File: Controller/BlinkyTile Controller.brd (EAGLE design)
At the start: 78 x 30 mm, 27 parts, among them IC1 74LVC1G17DCK, IC2 74LVC1G17DCK, Q1 CRYSTAL_4PAD2520, SW1 SPST_TACT-EVQQ2, SW2 SPST_TACT-EVQQ2, T1 TEST_PAD-7, T2 TEST_PAD-7, U1 MK20DX128VLF5

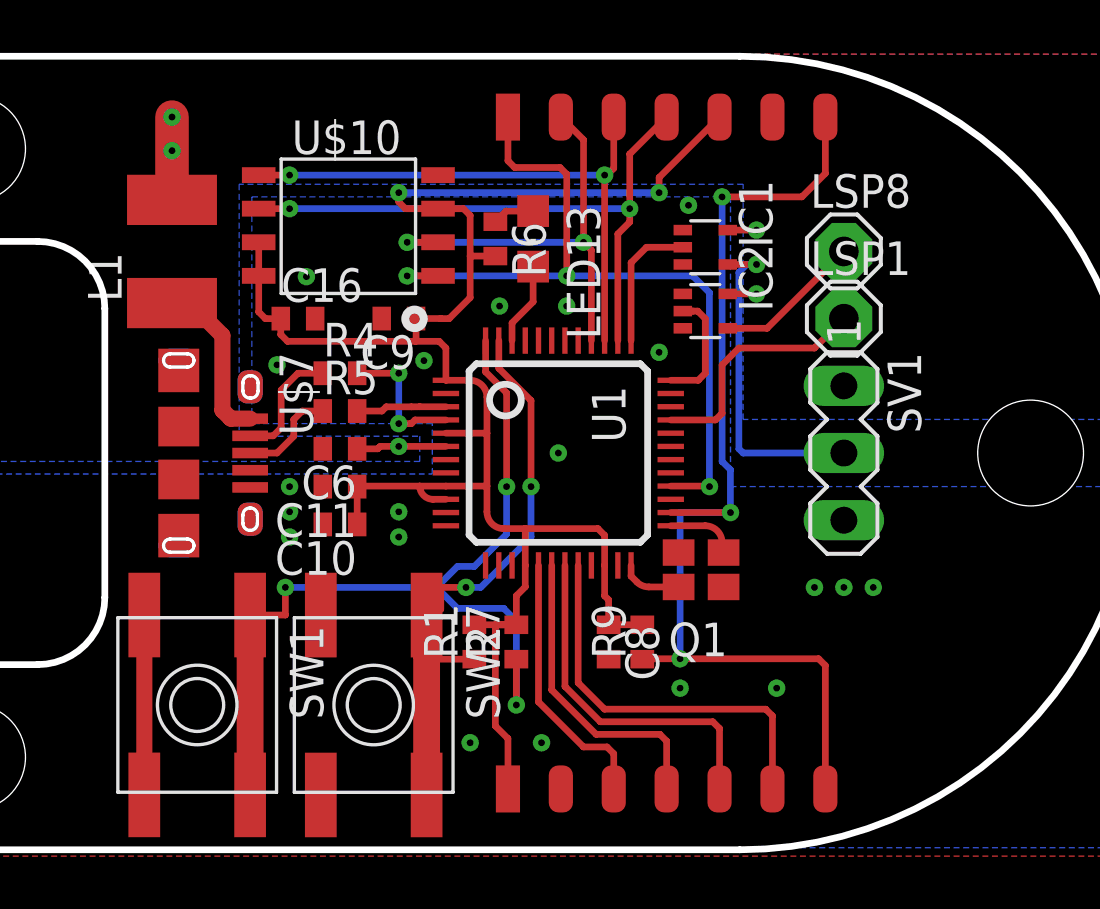
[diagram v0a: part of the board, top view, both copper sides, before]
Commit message: Update controller board design for RevA
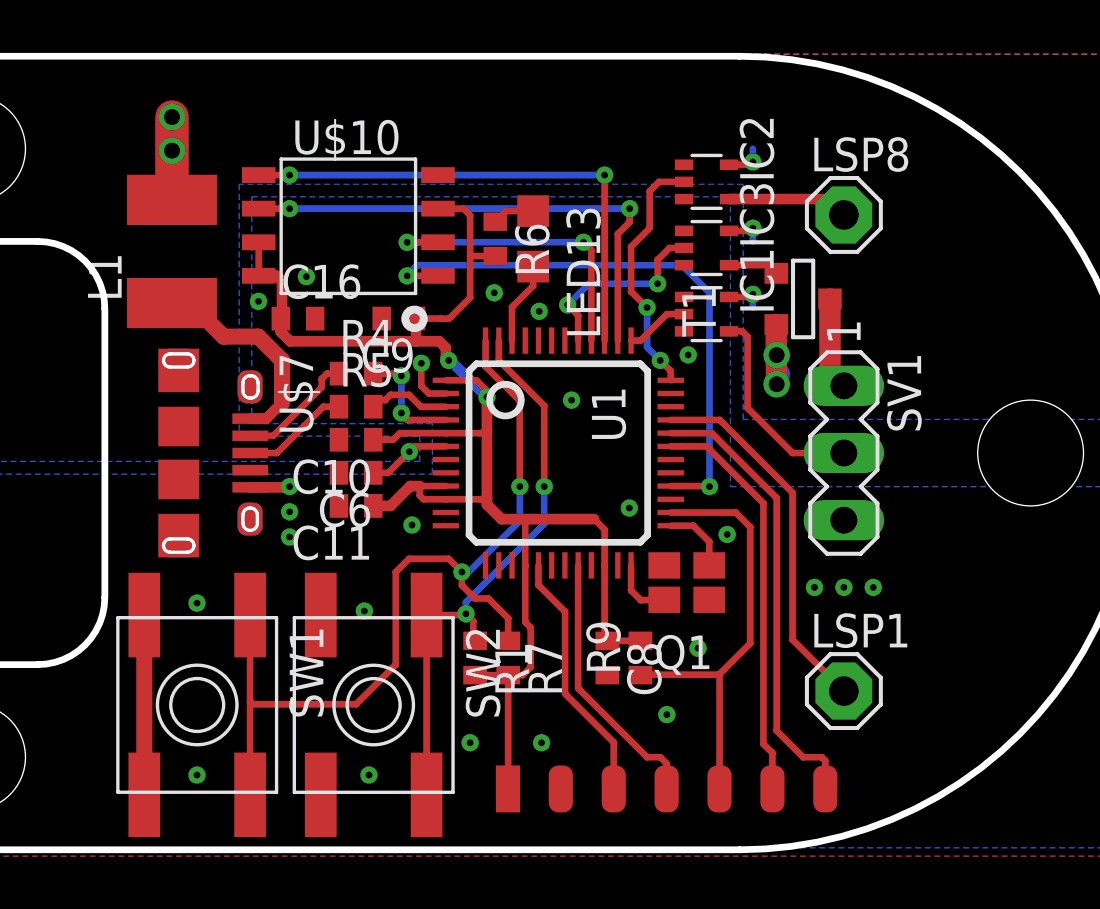
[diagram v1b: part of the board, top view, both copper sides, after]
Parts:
- added IC3: 74LVC1G17DCK, 74xx-little-us:SC70-5
- C10, C11, C16, C6, C8, C9: device rcl:C0402 -> adafruit:C0402
- R1, R4, R5, R6, R7, R9: device rcl:R0402 -> adafruit:R0402
- T1: value TEST_PAD-7 -> (none); device Sam Library:TEST_PAD-7 -> zetex:SOT-23
- moved LSP1 14.1 mm to (27.9, -9.00)
- moved T1 13.1 mm to (26.4, 5.80), turned to 90 degrees
- moved IC2 4.88 mm to (22.8, 10.2)
- moved C10 3.26 mm to (9.50, 0.50)
- moved IC1 2.53 mm to (22.8, 5.25)
- moved LSP8 1.38 mm to (27.9, 9.00)
- moved C6 1.09 mm to (9.50, -0.75)
- moved C11 0.95 mm to (9.50, -2.00)
- moved Q1 0.73 mm to (22.0, -4.90)
- moved R7 0.68 mm to (15.2, -7.75), turned to 270 degrees
- moved R5 0.63 mm to (9.50, 1.75)
- moved R9 0.61 mm to (20.2, -7.75)
- moved R4 0.61 mm to (9.50, 3.00)
- moved C8 0.61 mm to (19.0, -7.75)
- moved R1 0.61 mm to (14.0, -7.75), turned to 270 degrees
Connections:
- net ADDR_PROG renamed ADDRESS_PROGRAM
- new net N$5: SV1.1, T1.1
- new net N$6: IC3.4, T1.3
- new net POWER_ENABLE: IC3.2, U1.41
- net +3V3: no longer T1.5
- net +5V: now also IC3.5, T1.2; no longer SV1.1
- net FLASH_CS: no longer T1.1
- net FLASH_MISO: no longer T1.2
- net FLASH_MOSI: no longer T1.3
- net FLASH_SCK: no longer T1.4
- net GND: now also IC3.3; no longer T1.6
- net RESET: now also T2.5; no longer T1.7, T2.7
- net RX: now also T2.6
- net TDI: no longer T2.4
- net TDO: no longer T2.5
- net TMS: now also T2.4; no longer T2.6
- net TX: now also T2.7
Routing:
- net RESET: track 39.9 -> 16.6 mm, vias 3 -> 0
- net TX: track 0.00 -> 17.2 mm
- net RX: track 0.00 -> 15.3 mm
- net TDO: track 13.4 -> 0.00 mm
- net +3V3: track 73.4 -> 60.9 mm
- net TDI: track 11.7 -> 0.00 mm
- net FLASH_CS: track 29.6 -> 22.0 mm, vias 3 -> 2
- net POWER_ENABLE: track 0.00 -> 7.33 mm, vias 0 -> 2
- net FLASH_MISO: track 16.8 -> 11.7 mm
- net TMS: track 15.1 -> 10.1 mm
- net ADC1: track 9.20 -> 14.0 mm
- net LED_DATA: track 12.6 -> 7.83 mm, vias 1 -> 0
- net ADDRESS_PROGRAM: track 4.85 -> 9.51 mm, vias 0 -> 2
- net +5V: track 8.70 -> 13.3 mm, vias 5 -> 8
- net FLASH_SCK: track 23.2 -> 19.2 mm
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
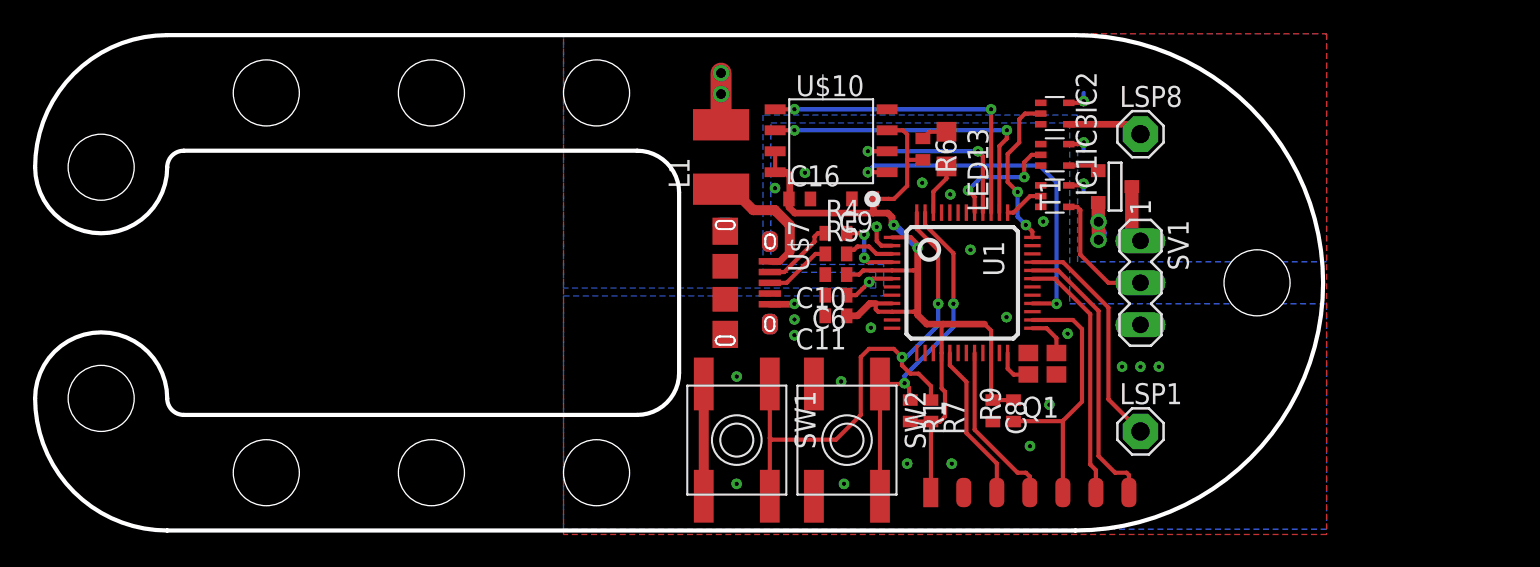
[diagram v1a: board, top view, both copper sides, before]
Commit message: Switch to smaller processor, change FLASH_CS to hardware CS pin
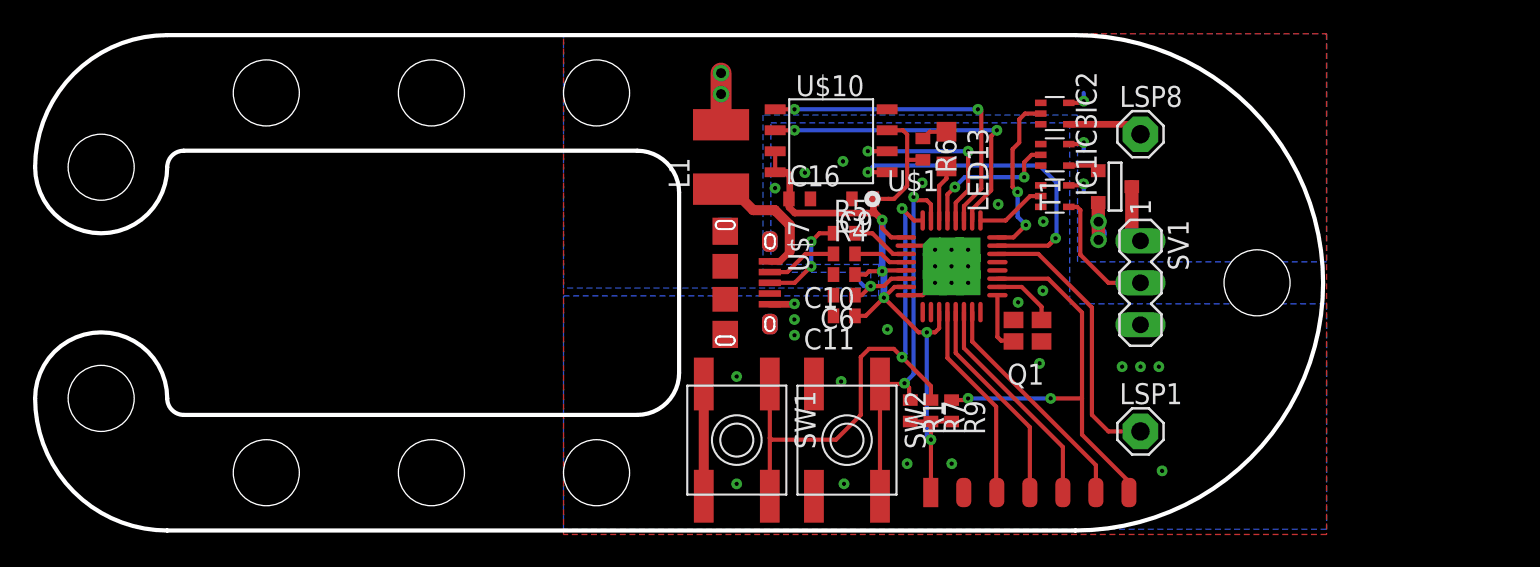
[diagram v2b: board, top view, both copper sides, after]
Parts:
- removed C8: 100nF, adafruit:C0402
- removed U1: MK20DX128VLF5, scanlime:LQFP48
- added U$1: MK20D--VFM5, blinkinlabs:QFN32_5X5_LONGLEADS
- moved R9 3.75 mm to (16.5, -7.75), turned to 270 degrees
- moved Q1 2.19 mm to (21.1, -2.90)
- moved R4 1.35 mm to (10.0, 1.75)
- moved R5 1.35 mm to (10.0, 3.00)
- moved C10 0.50 mm to (10.0, 0.50)
- moved C11 0.50 mm to (10.0, -2.00)
- moved C6 0.50 mm to (10.0, -0.75)
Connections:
- removed net ADC1: LSP1.MP, U1.33
- removed net TDI: U1.18
- removed net TDO: U1.19
- new net ADC15: LSP1.MP, U$1.22
- net +3V3: now also U$1.1, U$1.11, U$1.5, U$1.7; no longer C8.1, U1.1, U1.10, U1.16, U1.22, U1.5, U1.9
- net +5V: now also U$1.6; no longer U1.6
- net ADDRESS_PROGRAM: now also U$1.24; no longer U1.36
- net DATA_OUT: now also U$1.25; no longer U1.37
- net FLASH_CS: now also U$1.23; no longer U1.28
- net FLASH_MISO: now also U$1.28; no longer U1.40
- net FLASH_MOSI: now also U$1.27; no longer U1.39
- net FLASH_SCK: now also U$1.26; no longer U1.38
- net GND: now also U$1.2, U$1.8, U$1.PAD@1, U$1.PAD@10, U$1.PAD@11, U$1.PAD@2, U$1.PAD@3, U$1.PAD@4, U$1.PAD@5, U$1.PAD@6, U$1.PAD@9; no longer C8.2, U1.11, U1.12, U1.2, U1.23
- net N$1: now also U$1.18; no longer U1.25
- net N$11: now also U$1.4; no longer U1.4
- net N$12: now also U$1.3; no longer U1.3
- net N$2: now also U$1.17; no longer U1.24
- net POWER_ENABLE: now also U$1.29; no longer U1.41
- net RESET: now also T2.7, U$1.19; no longer T2.5, U1.26
- net RX: now also T2.4, U$1.13; no longer T2.6, U1.31
- net STATUS: now also U$1.30; no longer U1.46
- net SW1: now also U$1.32; no longer U1.48
- net SW2: now also U$1.31; no longer U1.47
- net TCLK: now also U$1.12; no longer U1.17
- net TMS: now also T2.6, U$1.15; no longer T2.4, U1.20
- net TX: now also T2.5, U$1.14; no longer T2.7, U1.32
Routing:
- net ADC15: track 0.00 -> 16.9 mm
- net ADC1: track 14.0 -> 0.00 mm
- net +3V3: track 60.9 -> 51.3 mm, vias 2 -> 5
- net RESET: track 16.6 -> 26.0 mm, vias 0 -> 2
- net TMS: track 10.1 -> 14.0 mm
- net TX: track 17.2 -> 13.4 mm
- net RX: track 15.3 -> 12.8 mm
- net TCLK: track 9.63 -> 12.2 mm
- net GND: track 10.2 -> 12.3 mm, vias 24 -> 23
- net N$10: track 4.08 -> 5.98 mm, vias 0 -> 2
- net DATA_OUT: track 2.42 -> 4.26 mm
- net SW2: track 22.4 -> 23.8 mm
- net POWER_ENABLE: track 7.33 -> 8.75 mm
- net N$1: track 2.60 -> 3.97 mm
- net N$2: track 2.35 -> 3.60 mm
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
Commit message: Update to RevB controller from Sam
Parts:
- removed C10: 2.2uF, adafruit:C0402
- removed C11, C16, C9: 100nF, adafruit:C0402
- removed IC1, IC2, IC3: 74LVC1G17DCK, 74xx-little-us:SC70-5
- removed LED13: (no value), adafruit:CHIPLED_0805
- removed LSP1, LSP8: SE11, solpad:SE11
- removed R7: 10k, adafruit:R0402
- removed R9: 1k, adafruit:R0402
- removed SV1: (no value), con-lstb:MA03-1
- removed T2: TEST_PAD-7, Sam Library:TEST_PAD-7
- removed U$1: MK20D--VFM5, blinkinlabs:QFN32_5X5_LONGLEADS
- removed U$10: W25Q80BV, Blinkin_Labs:SOIC8
- removed U$7: USB_MICROSMT+THRUHULE, blinkinlabs:USB_MICRO_THRUHOLE
- added C1, C2, C3, C5: 100nF, adafruit:C0402
- added C4: 2.2uF, adafruit:C0402
- added CON1: USB_MICROSMT+THRUHULE, blinkinlabs:USB_MICRO_THRUHOLE
- added CON2: F-2X04-DIL-100, con-headers-jp:DIL-100-2X04
- added CON3: (no value), con-lstb:MA03-1
- added LED1: STATUS, adafruit:CHIPLED_0805
- added R2: 33, adafruit:R0402
- added R3: 1k, adafruit:R0402
- added TP1: ADCIN, solpad:SE11
- added TP2: ADDRESS, solpad:SE11
- added U1: MK20D--VFM5, blinkinlabs:QFN32_5X5_LONGLEADS
- added U2: W25Q80BV, Blinkin_Labs:SOIC8
- added U3, U4, U5: 74LVC1G17DCK, 74xx-little-us:SC70-5
- R1: value 10k -> 33
- R4: value 33 -> 1k
- R5: value 33 -> 10k
- R6: value 1k -> 10k
- moved SW2 18.0 mm to (10.0, 8.50), turned to 180 degrees
- moved R5 12.4 mm to (14.8, -8.50), turned to 270 degrees
- moved R4 11.8 mm to (4.24, -8.60), turned to 90 degrees
- moved R1 10.8 mm to (8.38, 1.50), turned to 0 degrees
- moved SW1 6.59 mm to (10.0, -8.50), turned to 0 degrees
- moved C6 5.90 mm to (15.0, -3.88), turned to 90 degrees
- moved T1 4.01 mm to (26.1, 9.80)
- moved Q1 3.13 mm to (24.2, -3.02)
- moved R6 0.40 mm to (14.8, 8.50), turned to 90 degrees
- moved L1 0.24 mm to (2.75, 7.50)
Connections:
- new net PA4: CON2.8, U1.16
- net +3V3: now also C1.1, C2.1, C4.1, C5.1, C6.1, CON2.1, R3.2, R4.2, R5.2, U1.1, U1.11, U1.5, U1.7, U2.3, U2.7, U2.8; no longer C10.1, C11.1, C16.1, C9.1, R1.2, R7.2, R9.2, T2.1, U$1.1, U$1.11, U$1.5, U$1.7, U$10.3, U$10.7, U$10.8
- net +5V: now also C3.1, U1.6, U3.5, U4.5, U5.5; no longer C6.1, IC1.5, IC2.5, IC3.5, U$1.6
- net ADC15: now also TP1.MP, U1.22; no longer LSP1.MP, U$1.22
- net ADDRESS_PROGRAM: now also U1.24, U5.2; no longer IC2.2, U$1.24
- net DATA_OUT: now also U1.25, U4.2; no longer IC1.2, U$1.25
- net FLASH_CS: now also U1.23, U2.1; no longer U$1.23, U$10.1
- net FLASH_MISO: now also U1.28, U2.2; no longer U$1.28, U$10.2
- net FLASH_MOSI: now also U1.27, U2.5; no longer U$1.27, U$10.5
- net FLASH_SCK: now also U1.26, U2.6; no longer U$1.26, U$10.6
- net GND: now also C1.2, C2.2, C3.2, C4.2, C5.2, CON1.PIN$5, CON2.2, CON3.3, U1.2, U1.8, U1.PAD@1, U1.PAD@10, U1.PAD@11, U1.PAD@2, U1.PAD@3, U1.PAD@4, U1.PAD@5, U1.PAD@6, U1.PAD@9, U2.4, U3.3, U4.3, U5.3; no longer C10.2, C11.2, C16.2, C9.2, IC1.3, IC2.3, IC3.3, SV1.3, T2.2, U$1.2, U$1.8, U$1.PAD@1, U$1.PAD@10, U$1.PAD@11, U$1.PAD@2, U$1.PAD@3, U$1.PAD@4, U$1.PAD@5, U$1.PAD@6, U$1.PAD@9, U$10.4, U$7.PIN$5
- net LED_DATA: now also CON3.2, U4.4; no longer IC1.4, SV1.2
- net N$1: now also U1.18; no longer U$1.18
- net N$10: now also CON1.PIN$3, R2.1; no longer R5.1, U$7.PIN$3
- net N$11: now also R1.2, U1.4; no longer R4.2, U$1.4
- net N$12: now also R2.2, U1.3; no longer R5.2, U$1.3
- net N$16: now also LED1.A, R4.1; no longer LED13.A, R6.1
- net N$2: now also U1.17; no longer U$1.17
- net N$3: now also CON1.PIN$1; no longer U$7.PIN$1
- net N$4: now also TP2.MP, U5.4; no longer IC2.4, LSP8.MP
- net N$5: now also CON3.1; no longer SV1.1
- net N$6: now also U3.4; no longer IC3.4
- net N$9: now also CON1.PIN$2, R1.1; no longer R4.1, U$7.PIN$2
- net POWER_ENABLE: now also U1.29, U3.2; no longer IC3.2, U$1.29
- net RESET: now also CON2.7, R3.1, U1.19; no longer R9.1, T2.7, U$1.19
- net RX: now also CON2.4, U1.13; no longer T2.4, U$1.13
- net STATUS: now also LED1.C, U1.32; no longer LED13.C, U$1.30
- net SW1: now also R5.1, U1.31; no longer R7.1, U$1.32
- net SW2: now also R6.1, U1.30; no longer R1.1, U$1.31
- net TCLK: now also CON2.3, U1.12; no longer T2.3, U$1.12
- net TMS: now also CON2.6, U1.15; no longer T2.6, U$1.15
- net TX: now also CON2.5, U1.14; no longer T2.5, U$1.14
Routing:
- net +3V3: track 51.3 -> 80.2 mm, vias 5 -> 8
- net STATUS: track 3.45 -> 25.4 mm, vias 0 -> 2
- net FLASH_CS: track 20.9 -> 7.77 mm
- net +5V: track 14.3 -> 26.6 mm
- net FLASH_SCK: track 19.5 -> 8.24 mm, vias 2 -> 0
- net PA4: track 0.00 -> 8.71 mm
- net GND: track 12.3 -> 4.26 mm
- net RX: track 12.8 -> 4.87 mm
- net FLASH_MOSI: track 19.6 -> 11.8 mm
- net RESET: track 26.0 -> 18.2 mm, vias 2 -> 0
- net TMS: track 14.0 -> 6.67 mm
- net N$4: track 4.59 -> 11.8 mm
- net N$6: track 1.91 -> 9.06 mm, vias 0 -> 2
- net SW2: track 23.8 -> 17.0 mm, vias 2 -> 0
- net SW1: track 33.4 -> 27.1 mm
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- added copper zone on layer 16, net N$5
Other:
- board size 78 x 30 mm -> 35 x 25 mm
- board text added: "+5V"
- board text added: "3.3V"
- board text added: "ADC"
- board text added: "ADDRESS"
- board text added: "BlinkyTile Controller Rev B"
- board text added: "BlinkyTile.com"
- board text added: "DATA"
- board text added: "GND"
- board text added: "PA4"
- board text added: "RST"
- board text added: "RX"
- board text added: "TCLK"
- board text added: "TMS"
- board text added: "TX"

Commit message: Add extra vias for input power to the 5v mosfet
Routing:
- net +5V: track 26.6 -> 27.7 mm, vias 8 -> 9
- net PA4: track 8.71 -> 7.73 mm
- net TMS: track 6.67 -> 6.00 mm
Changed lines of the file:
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@@
 <vertex x="0.5" y="-4"/>
 </polygon>
-<rectangle x1="20.5" y1="-3.5" x2="21" y2="-2" layer="41"/>
+<rectangle x1="20.5" y1="-3" x2="21" y2="-2" layer="41"/>
 <rectangle x1="20.3" y1="-2" x2="20.5" y2="2" layer="41"/>
 <rectangle x1="16.5" y1="-2" x2="20.5" y2="-1.8" layer="41"/>
@@
 <text x="33.75" y="-2.5" size="0.6096" layer="25" rot="R90" align="center">GND</text>
 <text x="33.75" y="0" size="0.6096" layer="25" rot="R90" align="center">DATA</text>
-<text x="33.75" y="7.62" size="0.6096" layer="25" rot="R90" align="center">ADC</text>
-<text x="33.75" y="-7.62" size="0.6096" layer="25" rot="R90" align="center">ADDRESS</text>
+<text x="33.75" y="-7.38" size="0.6096" layer="25" rot="R90" align="center">ADC</text>
+<text x="33.75" y="7.38" size="0.6096" layer="25" rot="R90" align="center">ADDRESS</text>
 <text x="18" y="-11.25" size="0.4064" layer="25" rot="R180" align="center">3.3V</text>
 <text x="20.5" y="-11.25" size="0.4064" layer="25" rot="R180" align="center">TCLK</text>
@@
 <via x="24" y="0" extent="1-16" drill="0.254"/>
 <via x="23.875" y="4.125" extent="1-16" drill="0.254"/>
-<via x="26.5" y="-3.5" extent="1-16" drill="0.254"/>
+<via x="23" y="-4.75" extent="1-16" drill="0.254"/>
 <via x="10" y="5.25" extent="1-16" drill="0.254"/>
 <via x="13.375" y="-3.5" extent="1-16" drill="0.254"/>
@@
 <wire x1="26.85" y1="6.4" x2="26" y2="6.4" width="0.2032" layer="1"/>
 <via x="26" y="6.4" extent="1-16" drill="0.254"/>
-<wire x1="25.134" y1="8.8602" x2="26.1102" y2="8.8602" width="0.2032" layer="1"/>
-<wire x1="26.1102" y1="8.8602" x2="26.125" y2="8.875" width="0.2032" layer="1"/>
-<via x="26.125" y="8.875" extent="1-16" drill="0.254"/>
+<wire x1="25.134" y1="8.8602" x2="26.25" y2="8.8602" width="0.8128" layer="1"/>
+<wire x1="26.25" y1="8.8602" x2="26.25" y2="7.875" width="0.8128" layer="1"/>
+<via x="26.25" y="7.875" extent="1-16" drill="0.254"/>
 <wire x1="26.85" y1="3.9" x2="26" y2="3.9" width="0.2032" layer="1"/>
 <via x="26" y="3.9" extent="1-16" drill="0.254"/>
@@
 <wire x1="10.5" y1="-1.5" x2="10.625" y2="-1.625" width="0.2032" layer="1"/>
 <wire x1="10.625" y1="-1.625" x2="13.5" y2="-1.625" width="0.2032" layer="1"/>
+<via x="26.25" y="8.875" extent="1-16" drill="0.254"/>
 </signal>
 <signal name="+3V3">
@@
 <wire x1="19.75" y1="-2.775" x2="19.75" y2="-4.49" width="0.2032" layer="1"/>
 <wire x1="19.75" y1="-4.49" x2="20.385" y2="-5.125" width="0.2032" layer="1"/>
-<wire x1="20.385" y1="-5.125" x2="22.365" y2="-5.125" width="0.2032" layer="1"/>
-<wire x1="22.365" y1="-5.125" x2="23" y2="-5.76" width="0.2032" layer="1"/>
-<wire x1="23" y1="-5.76" x2="23" y2="-6.92" width="0.2032" layer="1"/>
 <wire x1="23" y1="-6.92" x2="23.01" y2="-6.93" width="0.2032" layer="1"/>
+<wire x1="20.385" y1="-5.125" x2="21.205" y2="-5.125" width="0.2032" layer="1"/>
+<wire x1="21.205" y1="-5.125" x2="23.01" y2="-6.93" width="0.2032" layer="1"/>
 </signal>
 <signal name="RX">
@@
 <wire x1="19.25" y1="-2.775" x2="19.25" y2="-4.99" width="0.2032" layer="1"/>
 <wire x1="19.25" y1="-4.99" x2="19.885" y2="-5.625" width="0.2032" layer="1"/>
-<wire x1="19.885" y1="-5.625" x2="21.115" y2="-5.625" width="0.2032" layer="1"/>
-<wire x1="21.115" y1="-5.625" x2="21.75" y2="-6.26" width="0.2032" layer="1"/>
-<wire x1="21.75" y1="-6.26" x2="21.75" y2="-8.21" width="0.2032" layer="1"/>
 <wire x1="21.75" y1="-8.21" x2="23.01" y2="-9.47" width="0.2032" layer="1"/>
+<wire x1="19.885" y1="-5.625" x2="20.875" y2="-5.625" width="0.2032" layer="1"/>
+<wire x1="20.875" y1="-5.625" x2="21.75" y2="-6.5" width="0.2032" layer="1"/>
+<wire x1="21.75" y1="-6.5" x2="21.75" y2="-8.21" width="0.2032" layer="1"/>
 </signal>
 <signal name="FLASH_CS">
@@
 <wire x1="20.25" y1="-2.775" x2="20.25" y2="-3.99" width="0.2032" layer="1"/>
 <wire x1="20.25" y1="-3.99" x2="20.885" y2="-4.625" width="0.2032" layer="1"/>
-<wire x1="20.885" y1="-4.625" x2="24.915" y2="-4.625" width="0.2032" layer="1"/>
-<wire x1="24.915" y1="-4.625" x2="25.55" y2="-5.26" width="0.2032" layer="1"/>
-<wire x1="25.55" y1="-5.26" x2="25.55" y2="-6.93" width="0.2032" layer="1"/>
+<wire x1="20.885" y1="-4.625" x2="21.625" y2="-4.625" width="0.2032" layer="1"/>
+<wire x1="21.625" y1="-4.625" x2="22.5" y2="-5.5" width="0.2032" layer="1"/>
+<wire x1="22.5" y1="-5.5" x2="24.12" y2="-5.5" width="0.2032" layer="1"/>
+<wire x1="24.12" y1="-5.5" x2="25.55" y2="-6.93" width="0.2032" layer="1"/>
 </signal>
 </signals>
